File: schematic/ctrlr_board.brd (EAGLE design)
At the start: 90.5 x 43.2 mm, 19 parts, among them K1 SRLY-19, K2 SRLY-19, K3 SRLY-19, K4 SRLY-19, K5 SRLY-19, K6 SRLY-19

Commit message: V1.0 of relay board
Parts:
- removed POWER: (no value), con-lstb:MA10-1
- added PWR: 10X1, dz:HDR10
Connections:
- net HOT: now also PWR.1; no longer POWER.1
- net N$10: now also PWR.6; no longer POWER.6
- net N$11: now also PWR.7; no longer POWER.7
- net N$12: now also PWR.2; no longer POWER.2
- net N$7: now also PWR.3; no longer POWER.3
- net N$8: now also PWR.4; no longer POWER.4
- net N$9: now also PWR.5; no longer POWER.5
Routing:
- net HOT: track 67.3 -> 191.8 mm
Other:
- board text added: "Raspberry Pi Relay Board"
- board text added: "V1.0"
- board text added: "©2012 Doug Zobel www.gelberhund.com"
- board text removed: "©2012 gelberhund.com"
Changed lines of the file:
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@@
 <layer number="19" name="Unrouted" color="6" fill="1" visible="yes" active="yes"/>
 <layer number="20" name="Dimension" color="15" fill="1" visible="yes" active="yes"/>
-<layer number="21" name="tPlace" color="7" fill="1" visible="yes" active="yes"/>
+<layer number="21" name="tPlace" color="15" fill="1" visible="yes" active="yes"/>
 <layer number="22" name="bPlace" color="7" fill="1" visible="yes" active="yes"/>
 <layer number="23" name="tOrigins" color="15" fill="1" visible="yes" active="yes"/>
 <layer number="24" name="bOrigins" color="15" fill="1" visible="yes" active="yes"/>
-<layer number="25" name="tNames" color="7" fill="1" visible="yes" active="yes"/>
-<layer number="26" name="bNames" color="7" fill="1" visible="yes" active="yes"/>
-<layer number="27" name="tValues" color="7" fill="1" visible="yes" active="yes"/>
-<layer number="28" name="bValues" color="7" fill="1" visible="yes" active="yes"/>
+<layer number="25" name="tNames" color="15" fill="1" visible="yes" active="yes"/>
+<layer number="26" name="bNames" color="6" fill="1" visible="yes" active="yes"/>
+<layer number="27" name="tValues" color="14" fill="1" visible="yes" active="yes"/>
+<layer number="28" name="bValues" color="6" fill="1" visible="yes" active="yes"/>
 <layer number="29" name="tStop" color="7" fill="3" visible="no" active="yes"/>
 <layer number="30" name="bStop" color="7" fill="6" visible="no" active="yes"/>
@@
 <layer number="43" name="vRestrict" color="2" fill="10" visible="yes" active="yes"/>
 <layer number="44" name="Drills" color="7" fill="1" visible="no" active="yes"/>
-<layer number="45" name="Holes" color="7" fill="1" visible="no" active="yes"/>
+<layer number="45" name="Holes" color="7" fill="1" visible="yes" active="yes"/>
 <layer number="46" name="Milling" color="3" fill="1" visible="no" active="yes"/>
 <layer number="47" name="Measures" color="7" fill="1" visible="no" active="yes"/>
@@
 <layer number="49" name="Reference" color="7" fill="1" visible="yes" active="yes"/>
 <layer number="50" name="dxf" color="7" fill="1" visible="no" active="no"/>
-<layer number="51" name="tDocu" color="7" fill="1" visible="yes" active="yes"/>
+<layer number="51" name="tDocu" color="14" fill="1" visible="yes" active="yes"/>
 <layer number="52" name="bDocu" color="7" fill="1" visible="yes" active="yes"/>
 <layer number="53" name="tGND_GNDA" color="7" fill="9" visible="no" active="no"/>
@@
 <wire x1="89.84" y1="40.63" x2="-0.635" y2="40.63" width="0" layer="20"/>
 <wire x1="-0.635" y1="40.63" x2="-0.635" y2="-2.54" width="0" layer="20"/>
-<text x="81.28" y="39.37" size="1.778" layer="26" rot="R270">©2012 gelberhund.com</text>
+<text x="22.86" y="39.37" size="1.778" layer="22" rot="MR180">©2012 Doug Zobel  www.gelberhund.com</text>
+<text x="19.05" y="-1.27" size="1.778" layer="22" rot="MR0">V1.0</text>
+<text x="68.58" y="19.05" size="1.778" layer="22" rot="MR0">Raspberry Pi  Relay Board</text>
 </plain>
 <attributes>
@@
 <elements>
 <element name="2803" library="uln-udn" package="DIL18" value="" x="6.35" y="10.16" rot="R270"/>
-<element name="POWER" library="con-lstb" package="MA10-1" value="" x="86.36" y="25.4" rot="R270">
-<attribute name="OC_NEWARK" value="unknown" x="25.4" y="-1.27" size="1.778" layer="27" rot="R270" display="off"/>
-<attribute name="MPN" value="" x="25.4" y="-1.27" size="1.778" layer="27" rot="R270" display="off"/>
-<attribute name="MF" value="" x="25.4" y="-1.27" size="1.778" layer="27" rot="R270" display="off"/>
-<attribute name="OC_FARNELL" value="unknown" x="25.4" y="-1.27" size="1.778" layer="27" rot="R270" display="off"/>
-</element>
 <element name="TEMP" library="dz" package="HDR3" value="3X1" x="6.35" y="36.83"/>
 <element name="RPI_HDR" library="dz" package="RASPBERRY_PI_HEADER" value="RASPBERRY_PI_HEADERRASPI_HDR" x="16.51" y="20.32"/>
@@
 <element name="RELAY6" library="dz" package="HDR2" value="2X1+-" x="78.74" y="1.27" rot="R180"/>
 <element name="K1" library="dz" package="OAC5" value="SRLY-19" x="25.4" y="19.05" rot="R90"/>
+<element name="PWR" library="dz" package="HDR10" value="10X1" x="86.36" y="25.4" rot="R270"/>
 </elements>
 <signals>
@@
 </signal>
 <signal name="HOT">
-<contactref element="POWER" pad="1"/>
 <contactref element="K2" pad="1"/>
 <contactref element="K3" pad="1"/>
@@
 <wire x1="43.18" y1="33.02" x2="53.34" y2="33.02" width="1.27" layer="1"/>
 <wire x1="53.34" y1="33.02" x2="63.5" y2="33.02" width="1.27" layer="1"/>
-<wire x1="63.5" y1="33.02" x2="73.66" y2="33.02" width="1.27" layer="1"/>
-<wire x1="73.66" y1="33.02" x2="73.66" y2="36.83" width="1.27" layer="1"/>
-<wire x1="73.66" y1="36.83" x2="86.36" y2="36.83" width="1.27" layer="1"/>
+<wire x1="63.5" y1="33.02" x2="72.39" y2="33.02" width="1.27" layer="1"/>
+<wire x1="72.39" y1="33.02" x2="73.66" y2="33.02" width="1.27" layer="1"/>
+<wire x1="73.66" y1="33.02" x2="73.66" y2="34.29" width="1.27" layer="1"/>
+<contactref element="PWR" pad="1"/>
+<wire x1="73.66" y1="34.29" x2="73.66" y2="35.56" width="1.27" layer="1"/>
+<wire x1="73.66" y1="35.56" x2="73.66" y2="36.83" width="1.27" layer="1"/>
+<wire x1="86.36" y1="36.83" x2="73.66" y2="36.83" width="1.27" layer="1"/>
+<wire x1="86.36" y1="38.1" x2="73.66" y2="38.1" width="1.27" layer="1"/>
+<wire x1="73.66" y1="38.1" x2="72.39" y2="38.1" width="1.27" layer="1"/>
+<wire x1="72.39" y1="38.1" x2="72.39" y2="34.29" width="1.27" layer="1"/>
+<wire x1="72.39" y1="34.29" x2="22.86" y2="34.29" width="1.27" layer="1"/>
+<wire x1="73.66" y1="38.1" x2="73.66" y2="36.83" width="1.27" layer="1"/>
+<wire x1="73.66" y1="34.29" x2="72.39" y2="34.29" width="1.27" layer="1"/>
+<wire x1="72.39" y1="34.29" x2="72.39" y2="33.02" width="1.27" layer="1"/>
+<wire x1="22.86" y1="35.56" x2="73.66" y2="35.56" width="1.27" layer="1"/>
+<wire x1="22.86" y1="35.56" x2="22.86" y2="33.02" width="1.27" layer="1"/>
 </signal>
 <signal name="N$7">
-<contactref element="POWER" pad="3"/>
 <contactref element="K2" pad="2"/>
 <wire x1="33.02" y1="22.86" x2="33.02" y2="27.94" width="1.27" layer="1"/>
 <wire x1="33.02" y1="27.94" x2="78.74" y2="27.94" width="1.27" layer="1"/>
 <wire x1="78.74" y1="27.94" x2="78.74" y2="31.75" width="1.27" layer="1"/>
-<wire x1="78.74" y1="31.75" x2="86.36" y2="31.75" width="1.27" layer="1"/>
+<contactref element="PWR" pad="3"/>
+<wire x1="86.36" y1="31.75" x2="78.74" y2="31.75" width="1.27" layer="1"/>
 </signal>
 <signal name="N$8">
-<contactref element="POWER" pad="4"/>
 <contactref element="K3" pad="2"/>
-<wire x1="86.36" y1="29.21" x2="81.28" y2="29.21" width="1.27" layer="1"/>
 <wire x1="81.28" y1="29.21" x2="81.28" y2="25.4" width="1.27" layer="1"/>
 <wire x1="81.28" y1="25.4" x2="43.18" y2="25.4" width="1.27" layer="1"/>
 <wire x1="43.18" y1="25.4" x2="43.18" y2="22.86" width="1.27" layer="1"/>
+<contactref element="PWR" pad="4"/>
+<wire x1="86.36" y1="29.21" x2="81.28" y2="29.21" width="1.27" layer="1"/>
 </signal>
 <signal name="N$9">
-<contactref element="POWER" pad="5"/>
 <contactref element="K4" pad="2"/>
 <wire x1="53.34" y1="22.86" x2="53.34" y2="27.94" width="1.27" layer="16"/>
 <wire x1="53.34" y1="27.94" x2="81.28" y2="27.94" width="1.27" layer="16"/>
 <wire x1="81.28" y1="27.94" x2="81.28" y2="26.67" width="1.27" layer="16"/>
-<wire x1="81.28" y1="26.67" x2="86.36" y2="26.67" width="1.27" layer="16"/>
+<contactref element="PWR" pad="5"/>
+<wire x1="86.36" y1="26.67" x2="81.28" y2="26.67" width="1.27" layer="16"/>
 </signal>
 <signal name="N$10">
-<contactref element="POWER" pad="6"/>
 <contactref element="K5" pad="2"/>
 <wire x1="63.5" y1="22.86" x2="63.5" y2="25.4" width="1.27" layer="16"/>
 <wire x1="63.5" y1="25.4" x2="78.74" y2="25.4" width="1.27" layer="16"/>
 <wire x1="78.74" y1="25.4" x2="78.74" y2="24.13" width="1.27" layer="16"/>
-<wire x1="78.74" y1="24.13" x2="86.36" y2="24.13" width="1.27" layer="16"/>
+<contactref element="PWR" pad="6"/>
+<wire x1="86.36" y1="24.13" x2="78.74" y2="24.13" width="1.27" layer="16"/>
 </signal>
 <signal name="N$11">
-<contactref element="POWER" pad="7"/>
 <contactref element="K6" pad="2"/>
-<wire x1="86.36" y1="21.59" x2="73.66" y2="21.59" width="1.27" layer="16"/>
 <wire x1="73.66" y1="21.59" x2="73.66" y2="22.86" width="1.27" layer="16"/>
+<contactref element="PWR" pad="7"/>
+<wire x1="73.66" y1="21.59" x2="86.36" y2="21.59" width="1.27" layer="16"/>
 </signal>
 <signal name="N$12">
-<contactref element="POWER" pad="2"/>
 <contactref element="K1" pad="2"/>
-<wire x1="86.36" y1="34.29" x2="76.2" y2="34.29" width="1.27" layer="1"/>
 <wire x1="76.2" y1="34.29" x2="76.2" y2="30.48" width="1.27" layer="1"/>
 <wire x1="76.2" y1="30.48" x2="22.86" y2="30.48" width="1.27" layer="1"/>
 <wire x1="22.86" y1="30.48" x2="22.86" y2="22.86" width="1.27" layer="1"/>
+<contactref element="PWR" pad="2"/>
+<wire x1="86.36" y1="34.29" x2="76.2" y2="34.29" width="1.27" layer="1"/>
 </signal>
 <signal name="RXD">

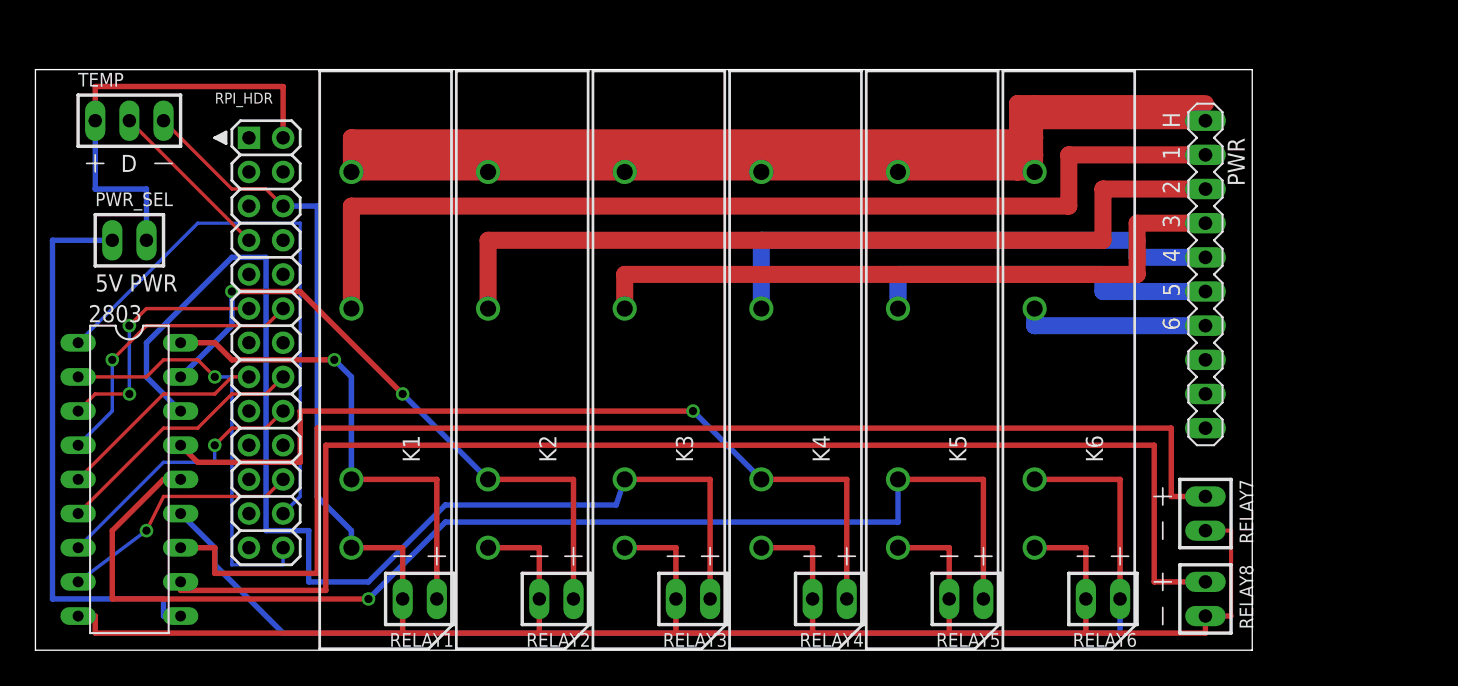
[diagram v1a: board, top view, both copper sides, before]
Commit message: Version 1.1 of expansion board
  * Rotated header 180 so expansion board sits over Rpi
  * re-wired relays to switch GND via darlingtons
  * Added optional SMD LEDs to relays 1-6 for testing
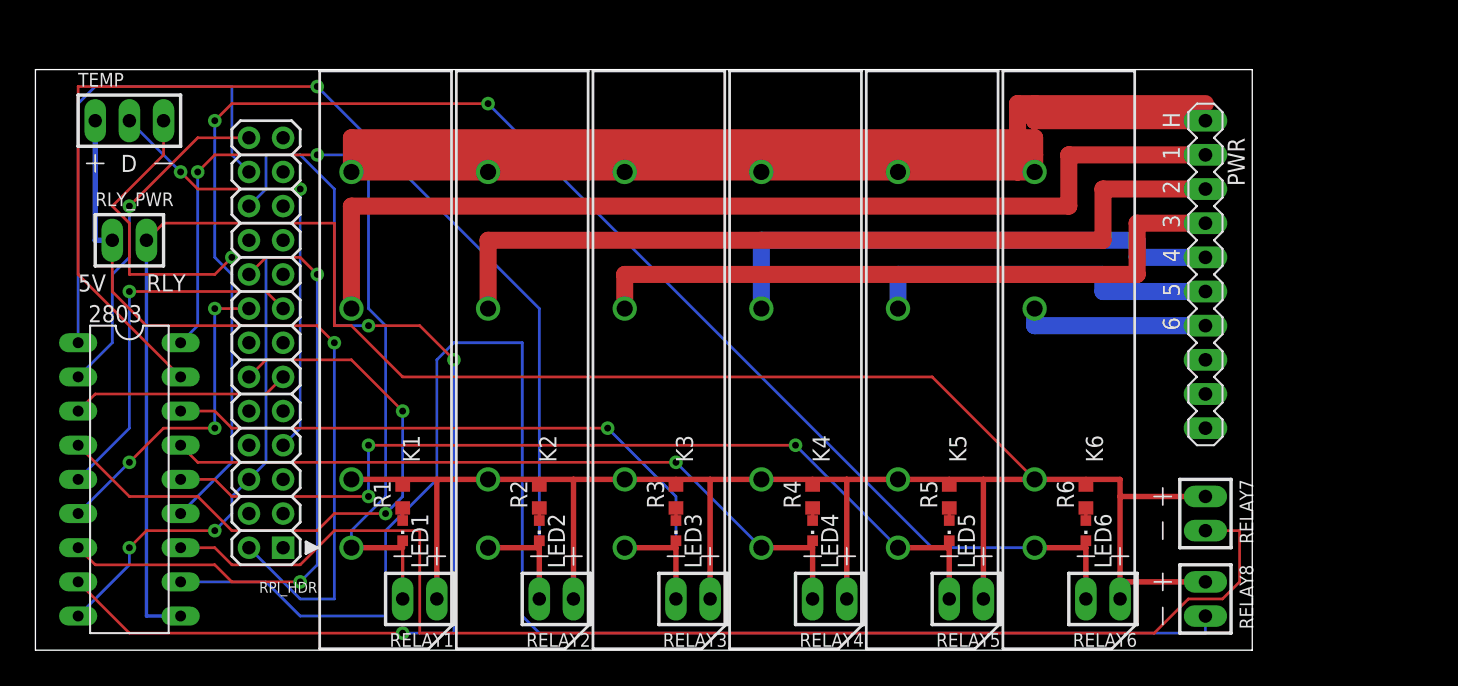
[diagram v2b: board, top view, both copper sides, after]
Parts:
- added LED1, LED2, LED3, LED4, LED5, LED6: (no value), led:CHIPLED_0603
- added R1, R2, R3, R4, R5, R6: (no value), resistor:R0603
- turned RPI_HDR to 180 degrees
- renumbered PWR_SEL to RLY_PWR
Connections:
- removed net PWR: 2803.10, RLY_PWR.+
- new net N$1: LED1.A, R1.1
- new net N$2: LED2.A, R2.1
- new net N$3: LED3.A, R3.1
- new net N$4: LED4.A, R4.1
- new net N$5: LED5.A, R5.1
- new net N$6: LED6.A, R6.1
- new net R_PWR: 2803.10, K1.3, K2.3, K3.3, K4.3, K5.3, K6.3, R1.2, R2.2, R3.2, R4.2, R5.2, R6.2, RELAY1.+, RELAY2.+, RELAY3.+, RELAY4.+, RELAY5.+, RELAY6.+, RELAY7.+, RELAY8.+, RLY_PWR.-
- net 5.0V: now also RLY_PWR.+; no longer RLY_PWR.-
- net GND: no longer K1.4, K2.4, K3.4, K4.4, K5.4, K6.4, RELAY1.-, RELAY2.-, RELAY3.-, RELAY4.-, RELAY5.-, RELAY6.-, RELAY7.-, RELAY8.-
- net O1: now also K1.4, LED1.C, RELAY1.-; no longer K1.3, RELAY1.+
- net O2: now also K2.4, LED2.C, RELAY2.-; no longer K2.3, RELAY2.+
- net O3: now also K3.4, LED3.C, RELAY3.-; no longer K3.3, RELAY3.+
- net O4: now also K4.4, LED4.C, RELAY4.-; no longer K4.3, RELAY4.+
- net O5: now also K5.4, LED5.C, RELAY5.-; no longer K5.3, RELAY5.+
- net O6: now also K6.4, LED6.C, RELAY6.-; no longer K6.3, RELAY6.+
- net O7: now also RELAY7.-; no longer RELAY7.+
- net O8: now also RELAY8.-; no longer RELAY8.+
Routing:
- net R_PWR: track 0.00 -> 235.1 mm
- net GND: track 198.0 -> 59.7 mm, vias 0 -> 3
- net GPIO25: track 18.6 -> 80.4 mm, vias 1 -> 3
- net O2: track 48.0 -> 95.6 mm, vias 2 -> 1
- net PWR: track 41.9 -> 0.00 mm
- net O3: track 87.4 -> 55.2 mm, vias 0 -> 1
- net O1: track 36.6 -> 65.4 mm, vias 1 -> 2
- net GPIO24: track 20.2 -> 47.1 mm, vias 1 -> 2
- net 5.0V: track 33.0 -> 59.0 mm, vias 0 -> 1
- net GPIO18: track 21.7 -> 47.7 mm, vias 1 -> 2
- net O6: track 92.1 -> 114.6 mm, vias 0 -> 2
- net O5: track 90.9 -> 69.0 mm, vias 1 -> 3
- net GPIO4: track 12.6 -> 34.4 mm, vias 0 -> 2
- net O8: track 97.8 -> 116.7 mm
- net GPIO22: track 15.9 -> 27.5 mm, vias 0 -> 1
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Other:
- board text added: "V1.1"
- board text removed: "V1.0"

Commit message: Version 1.1b of expansion board
  * v. 1.1 failed batchpcb DRC.
  * Re-did layout by hand
  * Added larger solder pads on relays
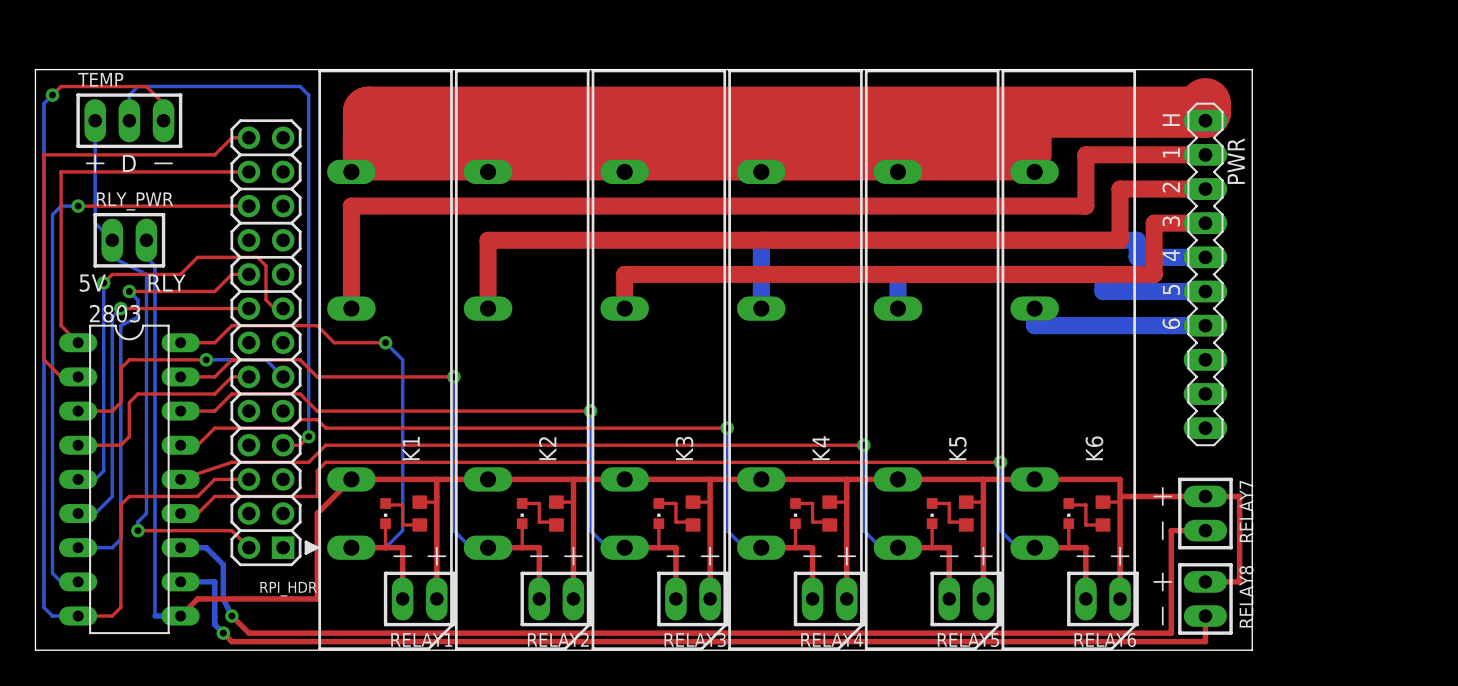
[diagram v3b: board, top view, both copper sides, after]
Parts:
- LED1, LED2, LED3, LED4, LED5, LED6: value (none) -> LED; device led:CHIPLED_0603 -> dz:LED0603
- R1, R2, R3, R4, R5, R6: value (none) -> 330; device resistor:R0603 -> dz:R0603
- moved LED1 1.80 mm to (25.4, 7.62)
- moved LED3 1.80 mm to (45.7, 7.62)
- moved R2 1.80 mm to (38.1, 7.62)
- moved R4 1.80 mm to (58.4, 7.62)
- moved R1 1.80 mm to (27.9, 7.62)
- moved LED2 1.80 mm to (35.6, 7.62)
- moved LED4 1.80 mm to (55.9, 7.62)
- moved LED5 1.80 mm to (66.0, 7.62)
- moved LED6 1.80 mm to (76.2, 7.62)
- moved R3 1.80 mm to (48.3, 7.62)
- moved R5 1.80 mm to (68.6, 7.62)
- moved R6 1.80 mm to (78.7, 7.62)
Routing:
- net HOT: track 191.8 -> 260.3 mm
- net O2: track 95.6 -> 45.3 mm
- net R_PWR: track 235.1 -> 189.1 mm
- net GPIO25: track 80.4 -> 43.7 mm, vias 3 -> 1
- net O8: track 116.7 -> 81.8 mm, vias 0 -> 1
- net O6: track 114.6 -> 81.2 mm, vias 2 -> 1
- net GPIO18: track 47.7 -> 16.3 mm, vias 2 -> 0
- net O1: track 65.4 -> 44.5 mm, vias 2 -> 1
- net 5.0V: track 59.0 -> 41.6 mm
- net GPIO24: track 47.1 -> 32.3 mm, vias 2 -> 1
- net GND: track 59.7 -> 72.9 mm, vias 3 -> 1
- net SPI_CE0: track 36.6 -> 27.2 mm
- net GPIO4: track 34.4 -> 43.3 mm, vias 2 -> 1
- net SPI_CE1: track 25.3 -> 34.1 mm, vias 1 -> 0
- net O7: track 95.9 -> 88.2 mm, vias 0 -> 1
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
